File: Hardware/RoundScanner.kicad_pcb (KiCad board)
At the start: 2 copper layers, 49.1 x 49.1 mm, 78 parts, among them J1 I2C Debug, J2 I2C, J3 I2C, Q1 BSS138DW-7-F, U1 OPA2376xxD, U2 NAU7802SGI, U3 LM285D-2.5, U4 TPS61023DRLR, U5 TLC59208FIPWR, U6 AS7341-DLGT, U7 AP7312-1833W6-7

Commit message: Added Logos
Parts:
- added REF**: OSHW-Logo_5.7x6mm_SilkScreen, Symbol:OSHW-Logo_5.7x6mm_SilkScreen, B.Cu at (89.3, 90.4)
- added REF**: PlasticScannerLogo, Symbol:PlasticScannerLogo, B.Cu at (89.3, 114.0)
- added kibuzzard-6346913B: G***, kibuzzard-6346913B, B.Cu at (89.3, 95.9)
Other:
- board text added: "HandheldScanner v0.1 2022-10-11"

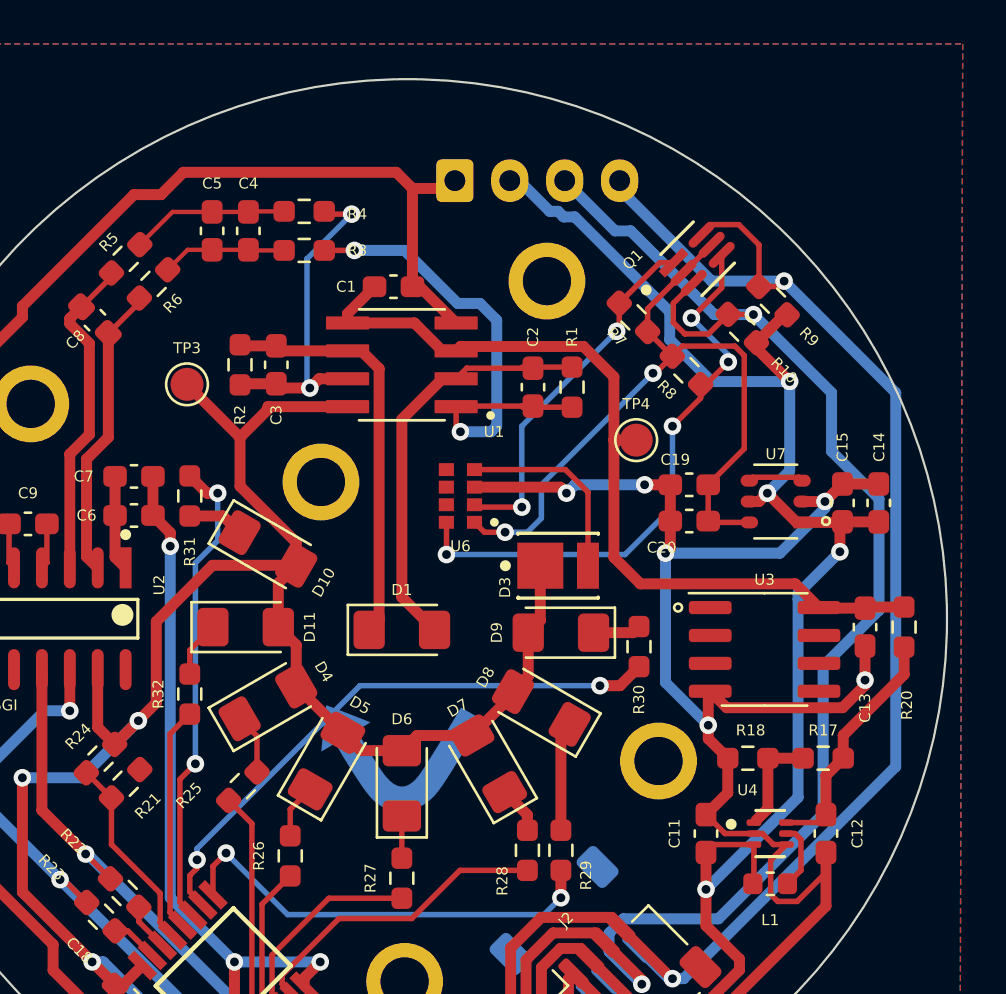
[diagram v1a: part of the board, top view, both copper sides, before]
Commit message: Added hole placement measurements
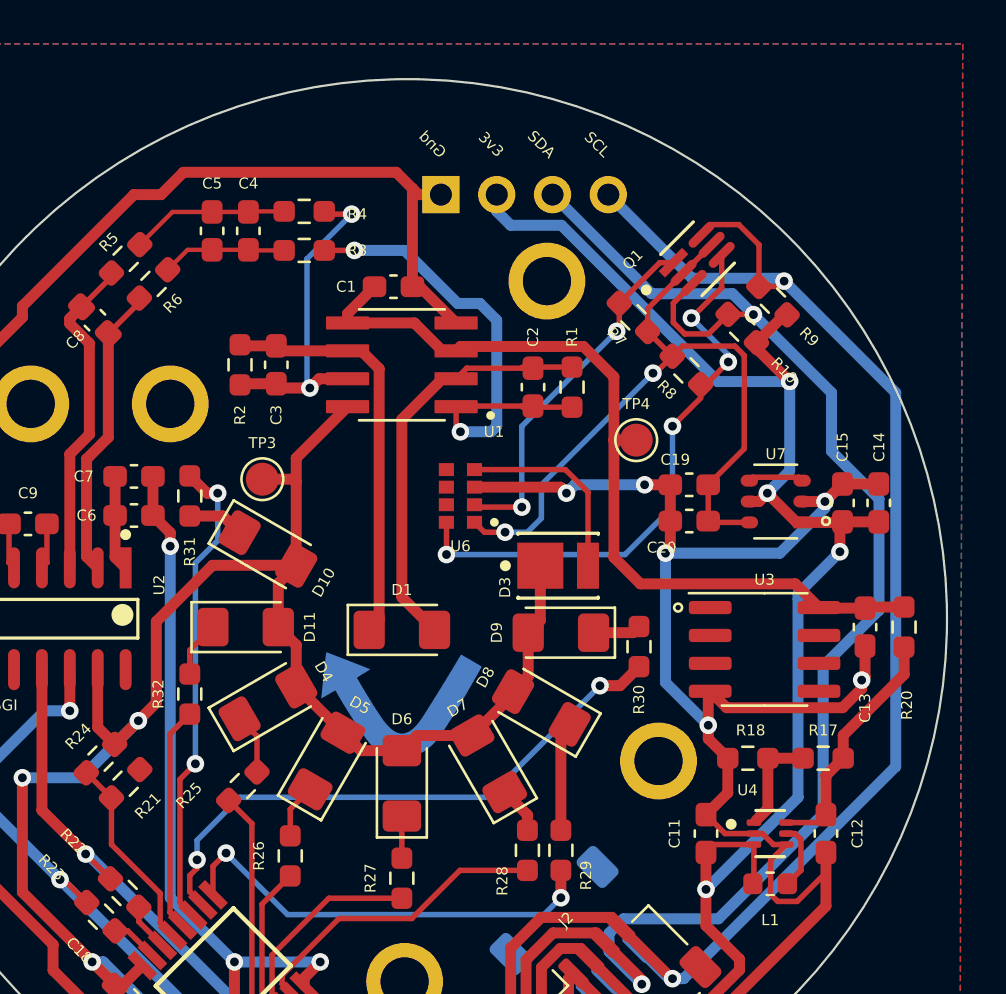
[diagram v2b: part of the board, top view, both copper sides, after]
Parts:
- removed the REF** at (89.3, 90.4)
- added REF**: OSHW-Logo2_7.3x6mm_SilkScreen, Symbol:OSHW-Logo2_7.3x6mm_SilkScreen, B.Cu at (89.3, 91.8)
- J1: footprint Connector_JST:JST_XH_B4B-XH-A_1x04_P2.50mm_Vertical -> Connector_PinHeader_2.54mm:PinHeader_1x04_P2.54mm_Vertical
- moved H2 7.73 mm to (78.7, 97.3)
- moved TP3 5.51 mm to (82.9, 100.7)
- moved REF** 2.41 mm to (89.3, 111.6)
- moved J1 0.90 mm to (91.1, 87.8), turned to -90 degrees
- moved kibuzzard-6346913B 0.89 mm to (89.3, 96.8)
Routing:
- net +3V3: track 181.5 -> 175.4 mm
- net GND: track 203.7 -> 203.1 mm
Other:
- board text added: "Gnd"
- board text removed: "ADCR"
- board text removed: "CS1"
- board text removed: "Greetings from"
- board text removed: "Markus"
- board text removed: "VCLK"
- board text removed: "VMISO"
- board text removed: "VMOSI"

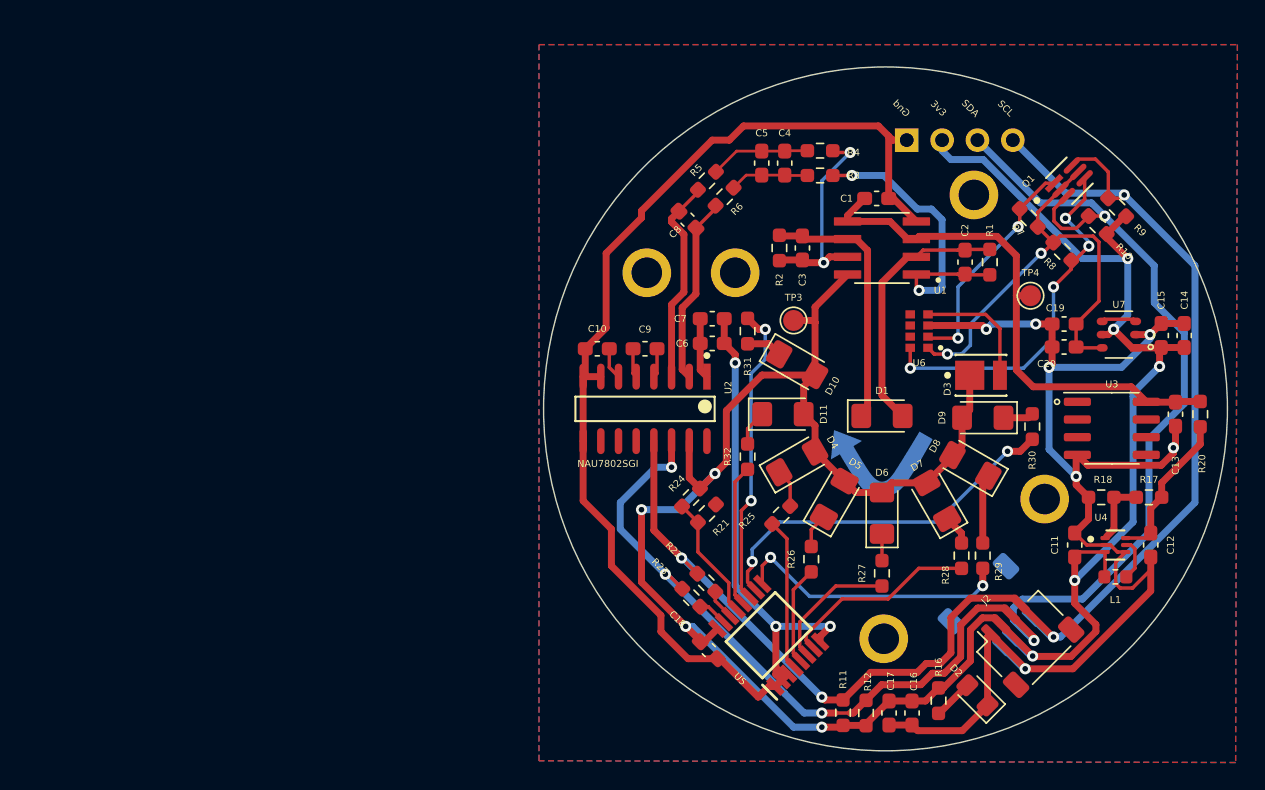
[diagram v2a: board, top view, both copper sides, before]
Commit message: removed TP561023, added footprint libraries
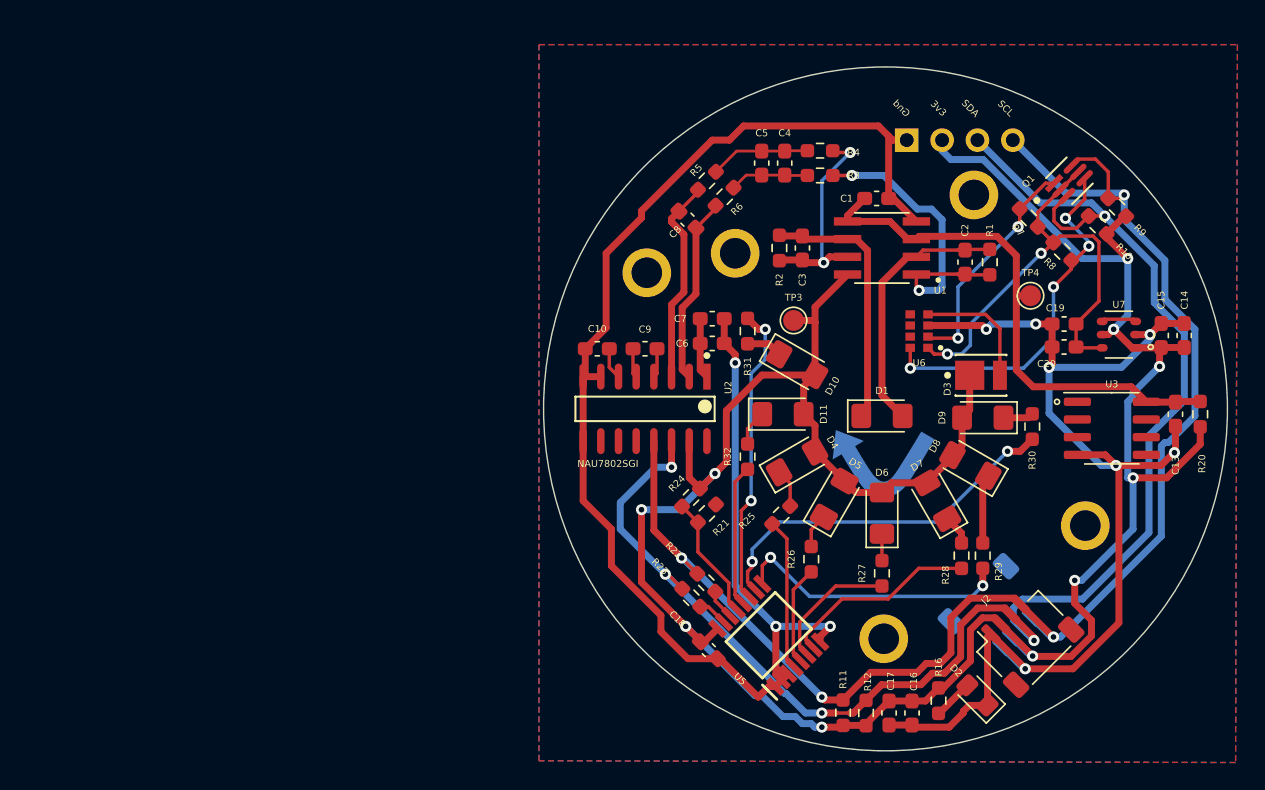
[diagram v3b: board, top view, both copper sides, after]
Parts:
- removed C11, C12: 2.2uF, Capacitor_SMD:C_0603_1608Metric_Pad1.08x0.95mm_HandSolder
- removed L1: INDUCTOR, Inductor_SMD:L_0603_1608Metric
- removed R17: 316k, Resistor_SMD:R_0603_1608Metric_Pad0.98x0.95mm_HandSolder
- removed R18: 100k, Resistor_SMD:R_0603_1608Metric_Pad0.98x0.95mm_HandSolder
- removed REF**: PlasticScannerLogo, Symbol:PlasticScannerLogo
- removed REF**: OSHW-Logo2_7.3x6mm_SilkScreen, Symbol:OSHW-Logo2_7.3x6mm_SilkScreen
- removed U4: TPS61023DRLR, TPS61023DRLR:Texas_Instruments_-_TPS61023DRLR
- added OSHSymbol: OSHW-Logo2_9.8x8mm_SilkScreen, PlasticScannerLibrary:OSHW-Logo2_9.8x8mm_SilkScreen, B.Cu at (89.3, 93.7)
- added PlasticScannerSymbol: PlasticScannerLogo, PlasticScannerLibrary:PlasticScannerLogo, B.Cu at (89.4, 111.6)
- C1, C10, C13, C14, C15, C16, C17, C18, C19, C2, C20, C3, C4, C5, C6, C7, C8, C9: footprint Capacitor_SMD:C_0603_1608Metric_Pad1.08x0.95mm_HandSolder -> PlasticScannerLibrary:C_0603_1608Metric_Pad1.08x0.95mm_HandSolder
- D1: footprint Diode_SMD:D_1206_3216Metric_Pad1.42x1.75mm_HandSolder -> PlasticScannerLibrary:D_1206_3216Metric_Pad1.42x1.75mm_HandSolder
- D10, D11, D4, D5, D6, D7, D8, D9: footprint LED_SMD:LED_1206_3216Metric_Pad1.42x1.75mm_HandSolder -> PlasticScannerLibrary:LED_1206_3216Metric_Pad1.42x1.75mm_HandSolder
- D2: footprint LED_SMD:LED_0805_2012Metric_Pad1.15x1.40mm_HandSolder -> PlasticScannerLibrary:LED_0805_2012Metric_Pad1.15x1.40mm_HandSolder
- D3: footprint Everlight-EAHC2835WD6:Everlight-EAHC2835WD6-MFG -> PlasticScannerLibrary:Everlight-EAHC2835WD6-MFG
- H1, H2, H3, H4, H5: footprint MountingHole:MountingHole_2.2mm_M2_ISO7380_Pad -> PlasticScannerLibrary:MountingHole_2.2mm_M2_ISO7380_Pad
- J1: footprint Connector_PinHeader_2.54mm:PinHeader_1x04_P2.54mm_Vertical -> PlasticScannerLibrary:PinHeader_1x04_P2.54mm_Vertical
- J2, J3: footprint Connector_JST:JST_SH_SM04B-SRSS-TB_1x04-1MP_P1.00mm_Horizontal -> PlasticScannerLibrary:JST_SH_SM04B-SRSS-TB_1x04-1MP_P1.00mm_Horizontal
- Q1: footprint BSS138DW-7-F-A:Diodes_Inc._-_BSS138DW-7-F-A -> PlasticScannerLibrary:Diodes_Inc._-_BSS138DW-7-F-A
- R1, R10, R11, R12, R16, R2, R21, R22, R23, R24, R25, R26, R27, R28, R29, R3, R30, R31, R32, R4, R5, R6, R7, R8, R9: footprint Resistor_SMD:R_0603_1608Metric_Pad0.98x0.95mm_HandSolder -> PlasticScannerLibrary:R_0603_1608Metric_Pad0.98x0.95mm_HandSolder
- R20: value 1k -> 435; footprint Resistor_SMD:R_0603_1608Metric_Pad0.98x0.95mm_HandSolder -> PlasticScannerLibrary:R_0603_1608Metric_Pad0.98x0.95mm_HandSolder
- TP3, TP4: footprint TestPoint:TestPoint_Pad_D1.5mm -> PlasticScannerLibrary:TestPoint_Pad_D1.5mm
- U1: footprint OPA2376AID:SOIC127P599X175-8N -> PlasticScannerLibrary:SOIC127P599X175-8N
- U2: footprint Nuvoton-NAU7802SGI:Nuvoton-NAU7802SGI -> PlasticScannerLibrary:Nuvoton-NAU7802SGI
- U3: footprint Package_SO:SOIC-8_3.9x4.9mm_P1.27mm -> PlasticScannerLibrary:SOIC-8_3.9x4.9mm_P1.27mm
- U5: footprint TLC59208FIPWR:SOP65P640X120-16N -> PlasticScannerLibrary:SOP65P640X120-16N
- U6: footprint AS7341-DLGT:PSON80P310X200X110-8N -> PlasticScannerLibrary:PSON80P310X200X110-8N
- U7: footprint AP7312-1833W6-7:AP7312-1833W6-7 -> PlasticScannerLibrary:AP7312-1833W6-7
- kibuzzard-6346913B: footprint kibuzzard-6346913B -> PlasticScannerLibrary:kibuzzard-6346913B
- moved H3 3.49 mm to (103.9, 115.4)
- moved kibuzzard-6346913B 3.18 mm to (89.2, 99.9)
- moved H2 1.40 mm to (78.7, 95.9)
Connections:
- R20 pad 1: Net-(C12-Pad1) -> +3V3
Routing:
- net Net-(C12-Pad1): track 12.4 -> 0.00 mm
- net GND: track 203.1 -> 192.3 mm
- net Net-(R17-Pad2): track 4.66 -> 0.00 mm
- net +3V3: track 175.4 -> 178.7 mm, vias 9 -> 10
- net Net-(L1-Pad2): track 3.04 -> 0.00 mm

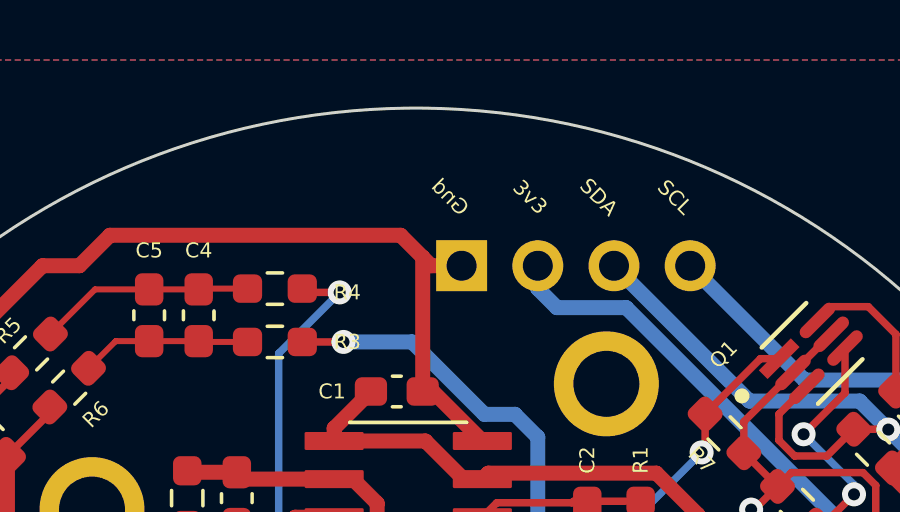
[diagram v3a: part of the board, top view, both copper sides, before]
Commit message: Edited 2.5v supply
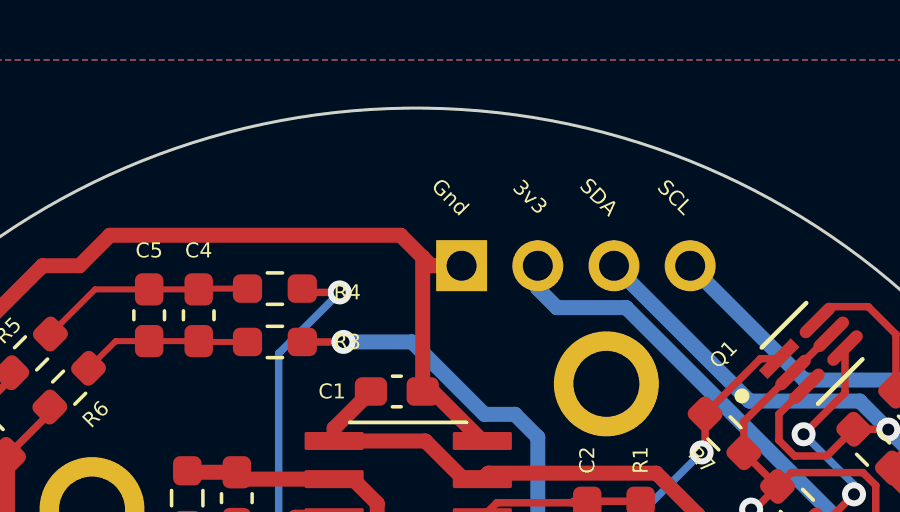
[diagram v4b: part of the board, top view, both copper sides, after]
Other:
- board text added: "HandheldScanner v0.3 2022-10-19"
- board text removed: "HandheldScanner v0.1 2022-10-11"
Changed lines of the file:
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@@
   (gr_circle (center 89.281 107.569) (end 105.638383 107.569) (layer "Cmts.User") (width 0.15) (fill none))
   (gr_circle locked (center 89.535 107.061) (end 114.046 108.585) (layer "Edge.Cuts") (width 0.1) (fill none))
-  (gr_text "HandheldScanner v0.1\n2022-10-11" (at 89.281 117.729) (layer "B.SilkS")
+  (gr_text "HandheldScanner v0.3\n2022-10-19" (at 89.281 117.729) (layer "B.SilkS")
     (effects (font (size 1 1) (thickness 0.15)) (justify mirror))
   )
@@
   )
   (gr_text "Gnd" (at 90.678 85.471 315) (layer "F.SilkS")
-    (effects (font (size 0.5 0.5) (thickness 0.1)) (justify mirror))
+    (effects (font (size 0.5 0.5) (thickness 0.1)))
   )
   (gr_text "SCL" (at 98.171 85.471 -45) (layer "F.SilkS")
@@
       (effects (font (size 1 1) (thickness 0.15)))
     )
-    (format (units 3) (units_format 1) (precision 4))
-    (style (thickness 0.15) (arrow_length 1.27) (text_position_mode 0) (extension_height 0.58642) (extension_offset 0.5) keep_text_aligned)
-  )
-  (dimension (type aligned) (layer "Cmts.User")
-    (pts (xy 89.281 107.569) (xy 89.281 97.282))
-    (height -29.845)
-    (gr_text "10.2870 mm" (at 58.286 102.4255 90) (layer "Cmts.User")
-      (effects (font (size 1 1) (thickness 0.15)))
-    )
-    (format (units 3) (units_format 1) (precision 4))
-    (style (thickness 0.15) (arrow_length 1.27) (text_position_mode 0) (extension_height 0.58642) (extension_offset 0.5) keep_text_aligned)
-  )
-  (dimension (type aligned) (layer "Cmts.User")
-    (pts (xy 89.281 107.569) (xy 89.281 113.538))
-    (height 29.718)
-    (gr_text "5.9690 mm" (at 58.413 110.5535 90) (layer "Cmts.User")
-      (effects (font (size 1 1) (thickness 0.15)))
-    )

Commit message: Updated power design
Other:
- board text added: "HandheldScanner v0.4 2022-10-19"
- board text removed: "HandheldScanner v0.3 2022-10-19"
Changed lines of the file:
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@@
   (gr_circle (center 89.281 107.569) (end 105.638383 107.569) (layer "Cmts.User") (width 0.15) (fill none))
   (gr_circle locked (center 89.535 107.061) (end 114.046 108.585) (layer "Edge.Cuts") (width 0.1) (fill none))
-  (gr_text "HandheldScanner v0.3\n2022-10-19" (at 89.281 117.729) (layer "B.SilkS")
+  (gr_text "HandheldScanner v0.4\n2022-10-19" (at 89.281 117.729) (layer "B.SilkS")
     (effects (font (size 1 1) (thickness 0.15)) (justify mirror))
   )

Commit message: Updated from discord feedback
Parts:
- removed OSHSymbol: OSHW-Logo2_9.8x8mm_SilkScreen, PlasticScannerLibrary:OSHW-Logo2_9.8x8mm_SilkScreen
- removed PlasticScannerSymbol: PlasticScannerLogo, PlasticScannerLibrary:PlasticScannerLogo
- removed R10, R9: 10k, PlasticScannerLibrary:R_0603_1608Metric_Pad0.98x0.95mm_HandSolder
- turned D3 to 0 degrees
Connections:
- D3 pad 1: +3V3 -> Net-(U6-Pad4)
- D3 pad 2: Net-(D3-Pad2) -> +3V3
- U6 pad 4: Net-(D3-Pad2) -> Net-(U6-Pad4)
- U6 pad 5: unconnected-(U6-Pad5) -> GND
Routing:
- net Net-(D3-Pad2): track 8.94 -> 0.00 mm
- net Net-(U6-Pad4): track 0.00 -> 8.50 mm
- net GND: track 192.3 -> 200.1 mm, vias 10 -> 11
- net +3V3: track 178.7 -> 171.4 mm, vias 10 -> 9
